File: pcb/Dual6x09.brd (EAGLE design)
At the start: 37.5 x 55.9 mm, 7 parts, among them IC1 6x09, IC2 6x09

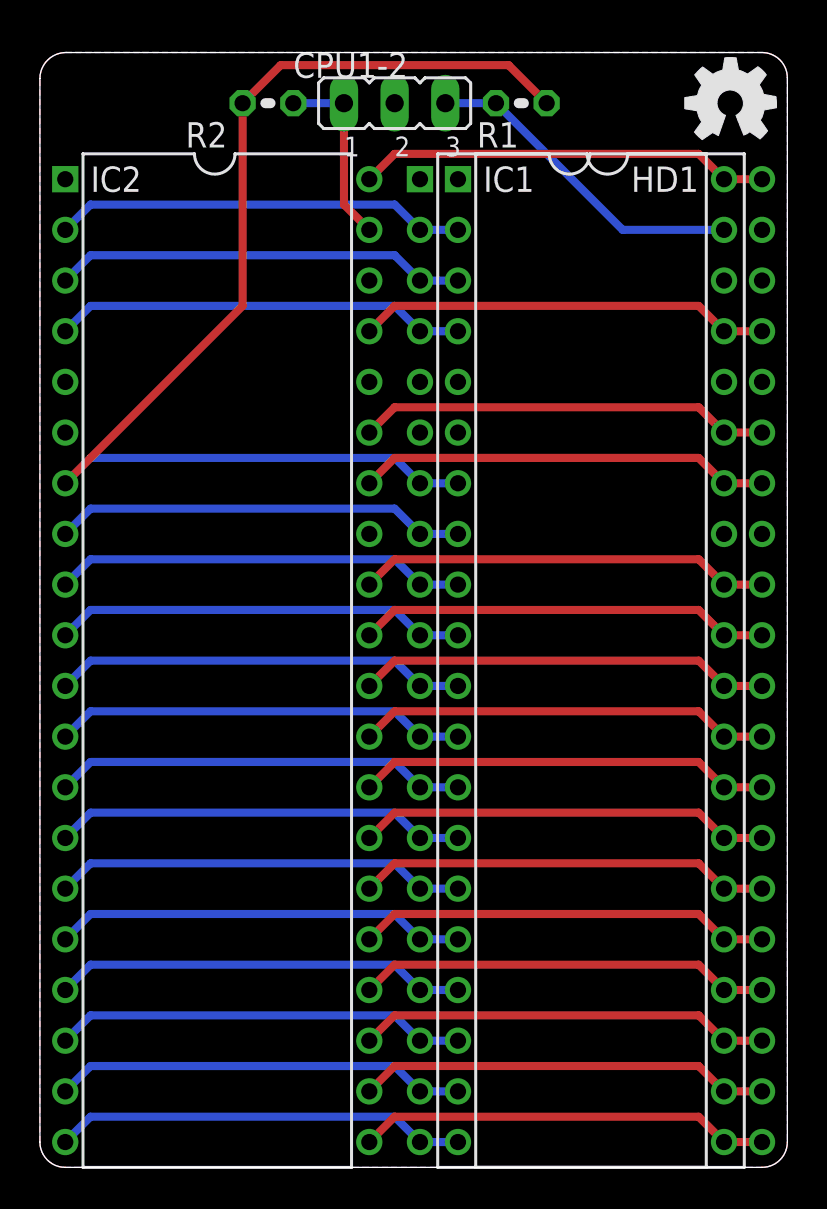
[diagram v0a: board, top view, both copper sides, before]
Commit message: Added DAT/MMU functionality support
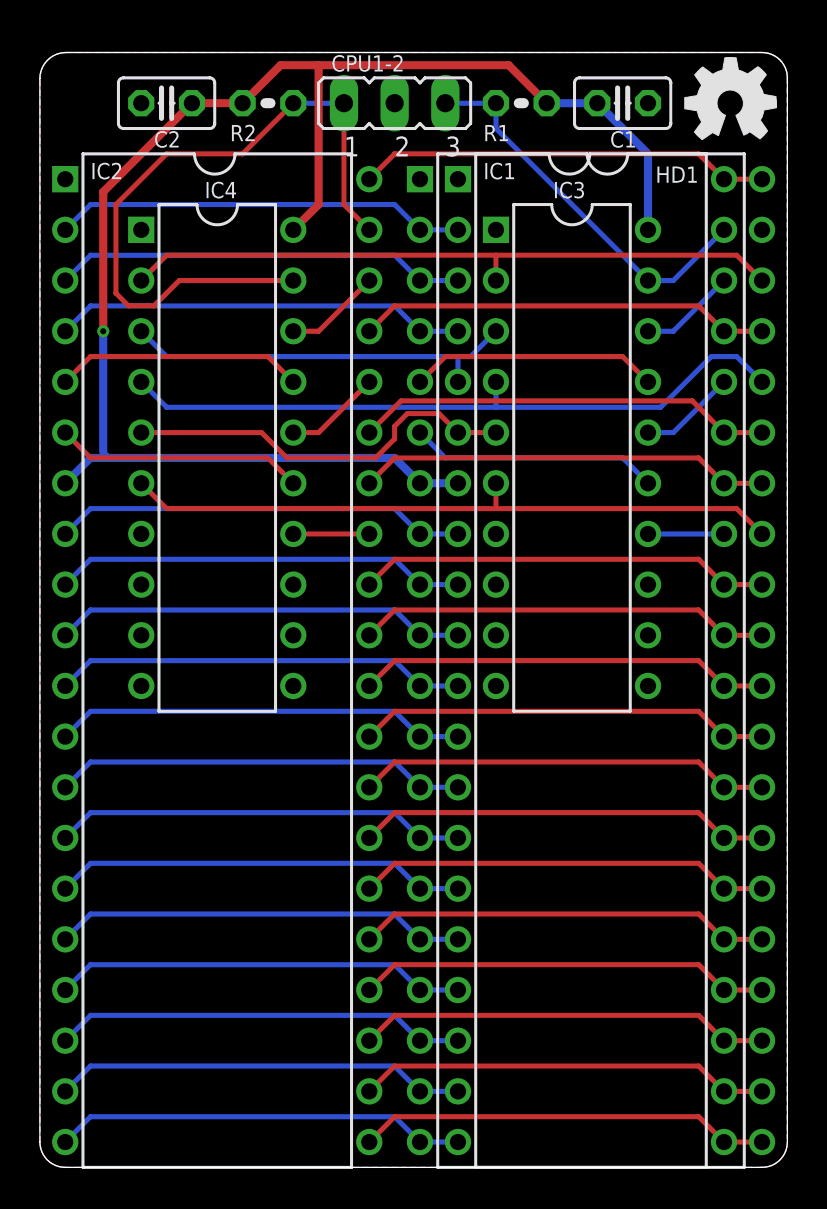
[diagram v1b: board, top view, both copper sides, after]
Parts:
- added C1, C2: (no value), rcl:C025-025X050
- added IC3, IC4: 74LS245N, 74xx-us-jlb:DIL20-RP
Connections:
- removed net N$1: CPU1-2.1, IC2.39, R2.1
- removed net N$2: CPU1-2.3, IC1.39, R1.1
- new net !CPU_1: CPU1-2.3, IC1.39, IC3.19, R1.1
- new net !CPU_2: CPU1-2.1, IC2.39, IC4.19, R2.1
- new net AVMA_1: IC1.36, IC3.16
- new net AVMA_2: IC2.36, IC4.16
- new net BA_1: IC1.6, IC3.15
- new net BA_2: IC2.6, IC4.15
- new net BS_1: IC1.5, IC3.17
- new net BS_2: IC2.5, IC4.17
- new net BUSY_1: IC1.33, IC3.14
- new net BUSY_2: IC2.33, IC4.14
- new net LIC_1: IC1.38, IC3.18
- new net LIC_2: IC2.38, IC4.18
- net AVMA: now also IC3.4, IC4.4
- net BA: now also IC3.5, IC4.5
- net BS: now also IC3.3, IC4.3
- net BUSY: now also IC3.6, IC4.6
- net GND: now also C1.2, C2.2, IC3.1, IC3.10, IC3.11, IC3.12, IC3.13, IC4.1, IC4.10, IC4.11, IC4.12, IC4.13
- net LIC: now also IC3.2, IC4.2
- net VCC: now also C1.1, C2.1, IC3.20, IC4.20
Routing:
- net !CPU_2: track 0.00 -> 34.5 mm
- net AVMA: track 0.00 -> 34.5 mm
- net LIC: track 0.00 -> 33.4 mm
- net BUSY: track 0.00 -> 33.4 mm
- net BS: track 0.00 -> 20.1 mm
- net BA: track 0.00 -> 20.0 mm
- net !CPU_1: track 0.00 -> 19.4 mm
- net VCC: track 60.3 -> 78.6 mm, vias 0 -> 1
- net N$2: track 16.6 -> 0.00 mm
- net BS_2: track 0.00 -> 12.5 mm
- net BS_1: track 0.00 -> 12.5 mm
- net BA_2: track 0.00 -> 12.5 mm
- net BA_1: track 0.00 -> 12.5 mm
- net N$1: track 9.42 -> 0.00 mm
- net LIC_2: track 0.00 -> 4.86 mm
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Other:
- board text added: "Dual6X09 (c) 2017-20 RETRO Innovations www.go4retro.com"
- board text removed: "(c) 2017 RETRO Innovations www.go4retro.com"
